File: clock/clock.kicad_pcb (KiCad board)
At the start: 2 copper layers, 176.8 x 81.3 mm, 341 parts, among them P101 CONN_01X03, P102 CONN_FAN_PWM, P103 XG4A-1631, P301 MCRF, P401 CONN_01X10, Q201 MMBT3904, Q301 BSS138, Q302 BSS138, Q401 BSS138, Q402 BSS138, Q501 BSS138, Q502 BSS138, U201 PCA9306, U202 DAC8830, U203 LMV722, U204 LTC2990, U205 LP3853, U207 NC7SZ125, U301 Adafruit746, U302 MIC5225, U303 PA6H, U401 74LVC541, U501 TPS56428, U502 TPS56428, U503 TPS56428, U601 ADT7410, U602 DS3231, U603 ADT7410, Y202 CX210

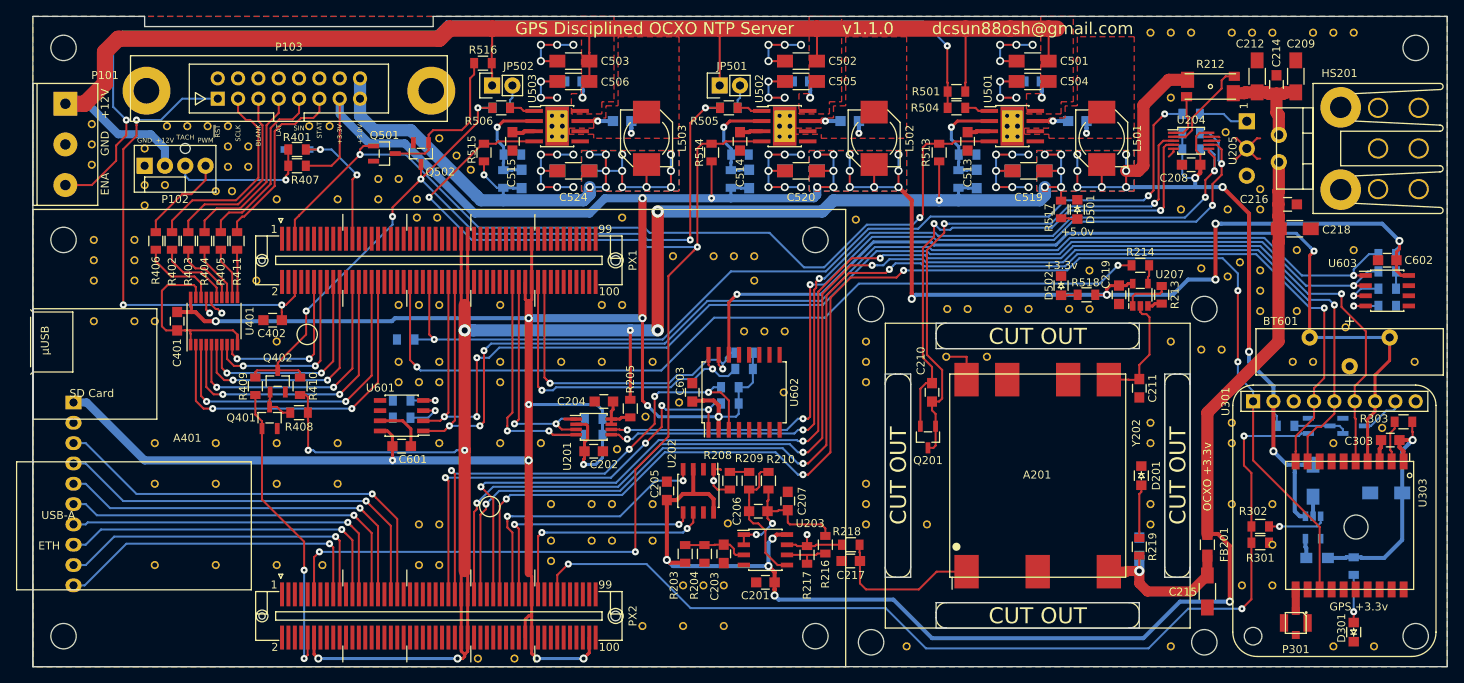
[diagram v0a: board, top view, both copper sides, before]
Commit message: Move power indicator LEDs. Clean up test points and silkscreen. Move the gate of Q302 to the other side of R301.
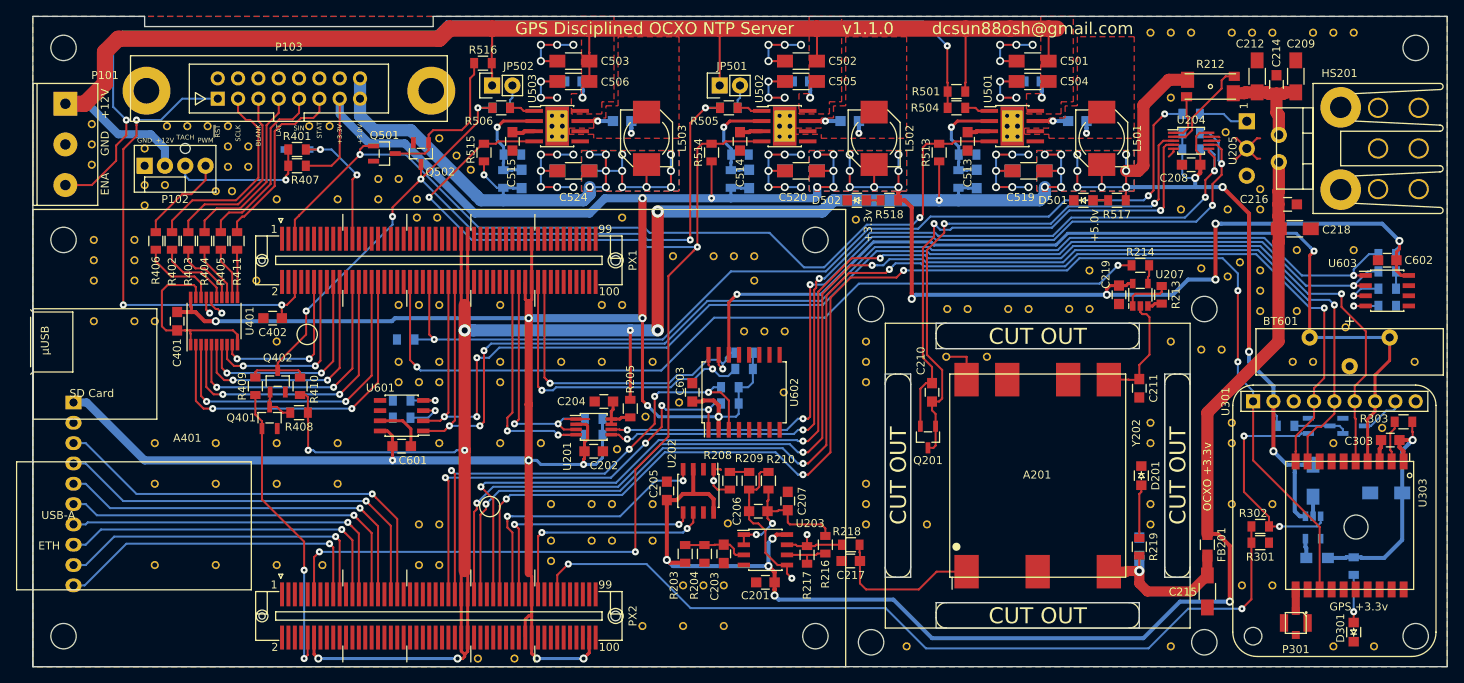
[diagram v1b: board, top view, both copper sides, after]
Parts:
- removed the REF** at (345.4, 231.1)
- moved D502 27.7 mm to (293.5, 188.1), turned to 0 degrees
- moved R518 27.3 mm to (297.6, 188.1)
- moved R517 7.08 mm to (326.0, 188.1), turned to 180 degrees
- moved D501 1.37 mm to (321.8, 188.1), turned to 0 degrees
- moved C402 0.25 mm to (220.5, 202.8)
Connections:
- Q302 pad 1: /gps/ENA -> /gps/ENABLE
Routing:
- net /gps/ENABLE: track 7.47 -> 28.2 mm, vias 1 -> 2
- net /gps/ENA: track 125.6 -> 105.8 mm, vias 3 -> 2
- net VCC: track 490.2 -> 485.8 mm, vias 30 -> 29
- net /ocxo/DAC_OUT_DIV: track 16.8 -> 18.7 mm, vias 0 -> 1
- net GND: track 141.9 -> 143.6 mm
- net /microzed/OCXO_SDA: track 32.4 -> 31.1 mm
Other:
- board text added: "DAC_OUT_DIV"
- board text added: "~RTC_INT~"

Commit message: Connect temperature sensor interrupt to FPGA.
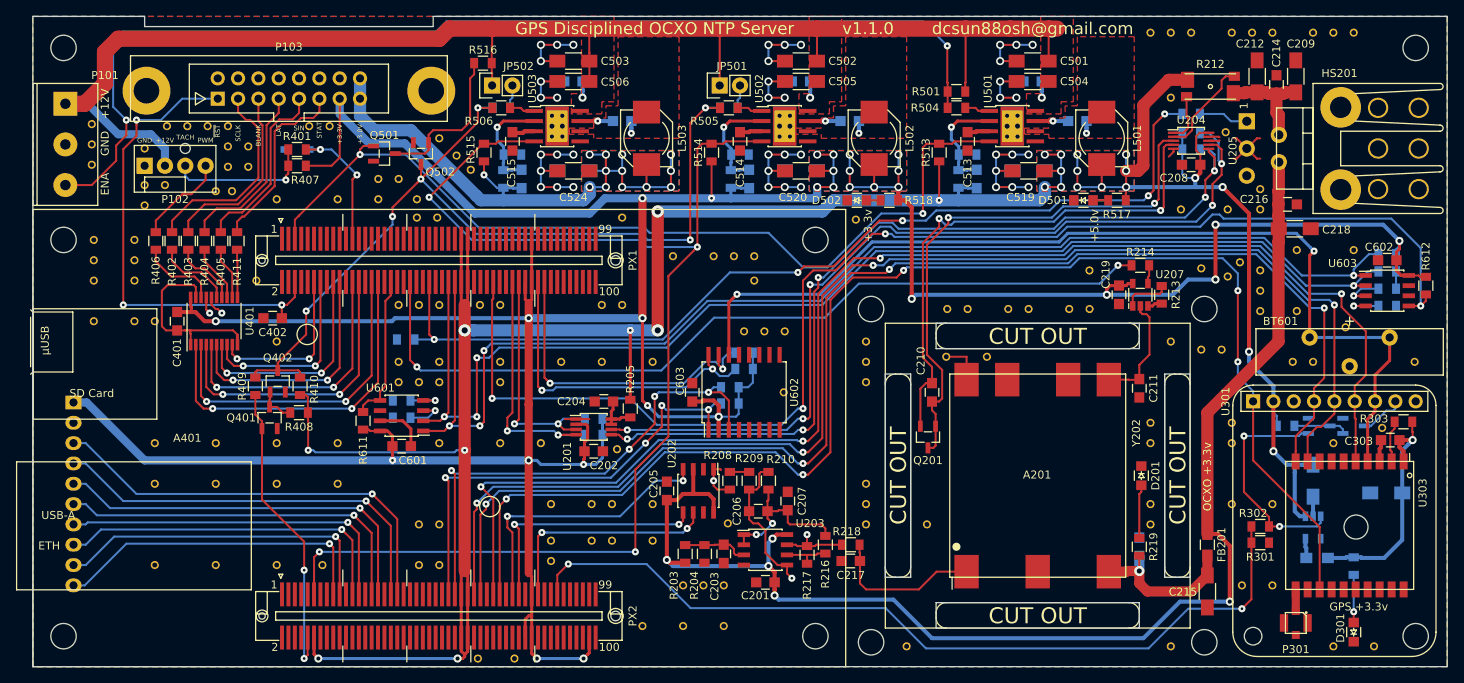
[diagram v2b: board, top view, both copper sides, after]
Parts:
- removed the REF** at (271.3, 213.4)
- removed the REF** at (267.1, 215.1)
- added R611: 1.00K, local:R_0805_HandSoldering, F.Cu at (231.8, 215.6)
- added R612: 1.00K, local:R_0805_HandSoldering, F.Cu at (364.6, 198.8)
- added REF**: Stitching_Via_40x24mil, local:Stitching_Via_40x24mil, F.Cu at (246.4, 201.2)
- R609, R610: value 10.0K -> 1.00K
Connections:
- net /rtctemp/~INT~ renamed /microzed/~INT~0
- PX1 pad 36: /microzed/PX1_LVDS_9_P -> /microzed/~INT~1
- PX1 pad 68: /microzed/PX1_LVDS_19_P -> /microzed/~INT~2
- U601 pad 5: Net-(U601-Pad5) -> /microzed/~INT~1
- U603 pad 5: Net-(U603-Pad5) -> /microzed/~INT~2
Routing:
- net /microzed/~INT~2: track 0.00 -> 164.8 mm, vias 0 -> 4
- net /microzed/~INT~1: track 0.00 -> 18.6 mm
- net VCC: track 485.8 -> 490.0 mm
- net /ocxo/ENA: vias 3 -> 5

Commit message: Clean up some of the trace routing. Update gerber files.
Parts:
- added REF**: Stitching_Via_40x24mil, local:Stitching_Via_40x24mil, F.Cu at (256.5, 201.2)
- added REF**: Stitching_Via_40x24mil, local:Stitching_Via_40x24mil, F.Cu at (229.9, 180.3)
- moved R217 2.41 mm to (289.7, 232.4)
- moved R216 2.29 mm to (287.3, 231.1)
- moved R206 0.25 mm to (237.1, 205.7)
- moved C217 0.13 mm to (292.9, 233.2)
- moved R218 0.13 mm to (292.9, 231.1)
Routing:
- net GND: track 143.6 -> 161.8 mm
- net /ocxo/BUF_VGND_1.65V: track 20.0 -> 17.6 mm
- net VXO: track 165.4 -> 163.2 mm
- net VCC: track 490.0 -> 488.7 mm
- net /ocxo/DAC_OUT: track 5.26 -> 4.29 mm
- net /power/+3.0V: track 76.9 -> 76.1 mm
- net VIN: track 352.4 -> 351.6 mm

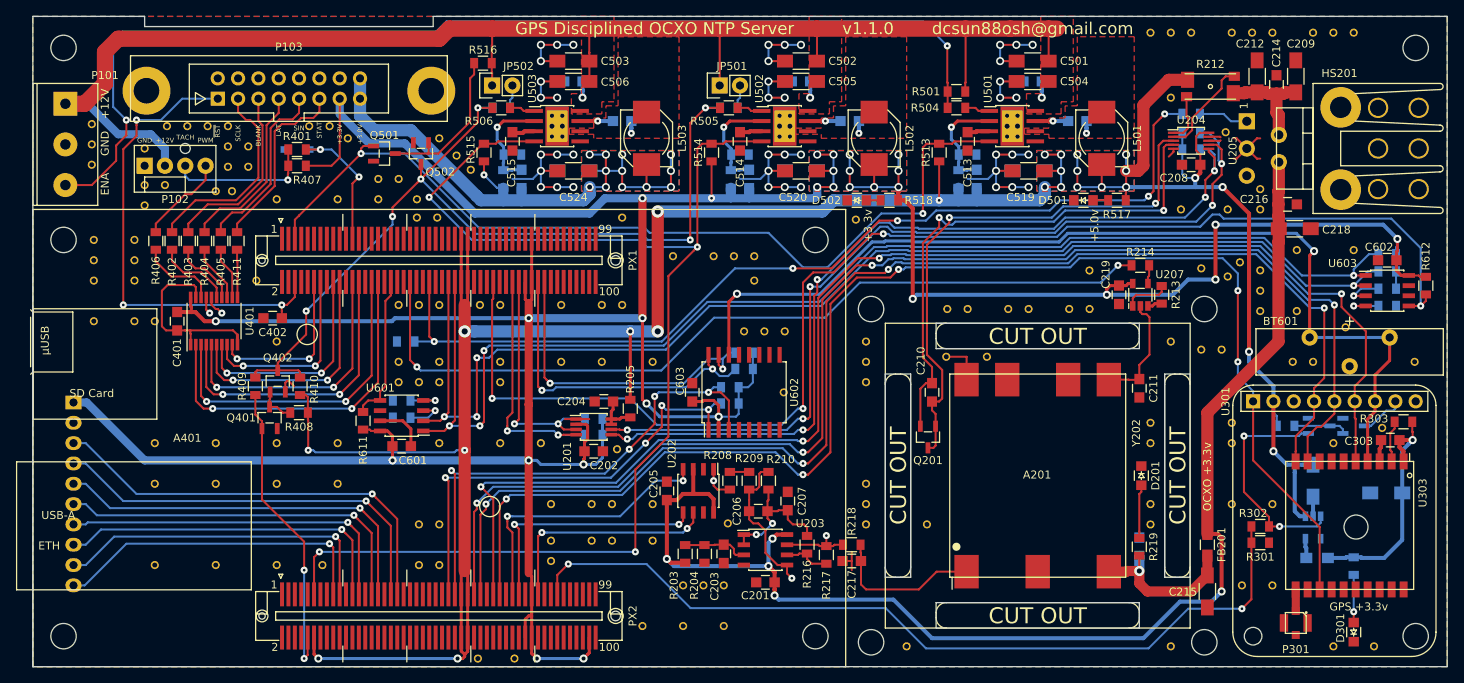
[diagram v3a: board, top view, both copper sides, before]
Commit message: Improve clearance around mounting hole.
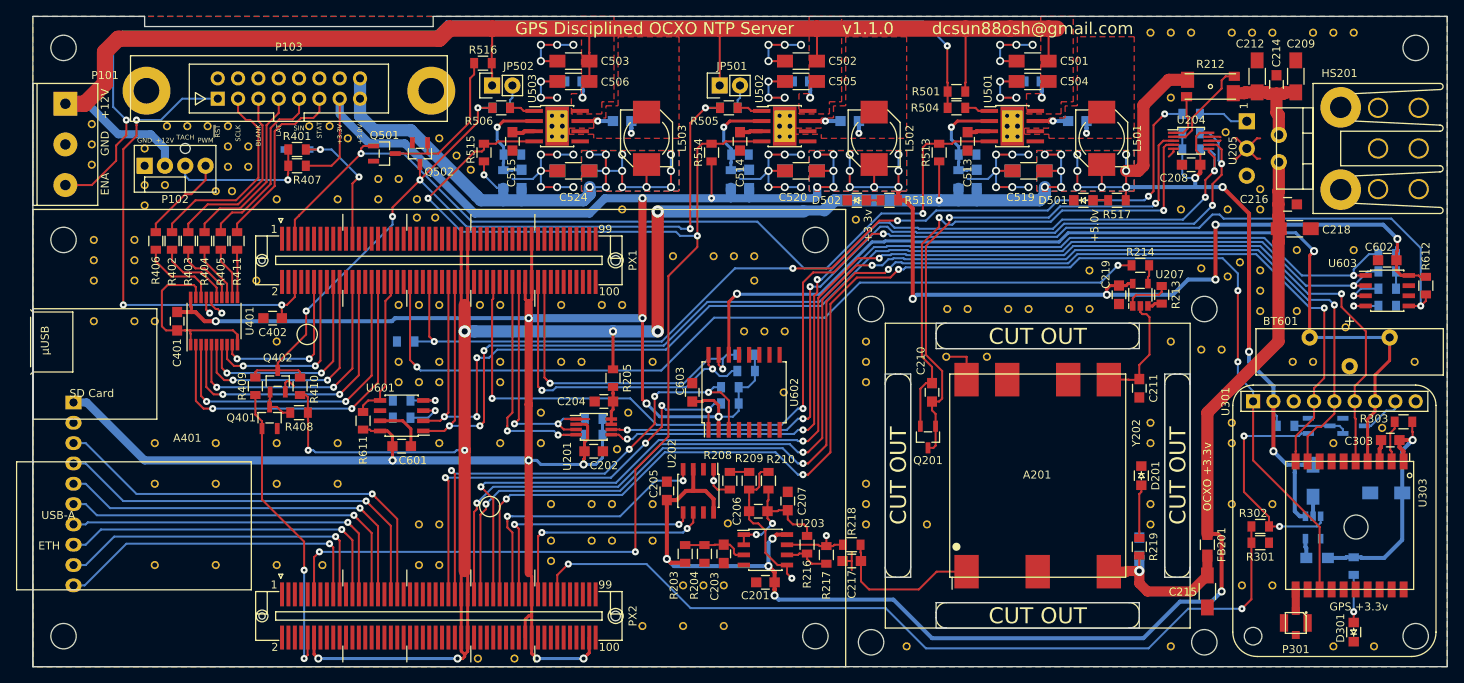
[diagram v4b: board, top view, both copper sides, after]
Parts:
- removed the REF** at (264.2, 190.2)
- added REF**: Stitching_Via_40x24mil, local:Stitching_Via_40x24mil, F.Cu at (264.2, 189.2)
- added REF**: Stitching_Via_40x24mil, local:Stitching_Via_40x24mil, F.Cu at (254.0, 214.6)
- added REF**: Stitching_Via_40x24mil, local:Stitching_Via_40x24mil, F.Cu at (264.9, 214.6)
- moved R205 4.38 mm to (263.0, 210.3)
- moved REF** 2.54 mm to (259.1, 208.3)
- moved R603 0.36 mm to (279.7, 207.4)
- moved R604 0.36 mm to (279.7, 209.4)
- moved REF** 0.25 mm to (240.8, 190.2)
- moved Q502 0.13 mm to (238.9, 182.2)
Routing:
- net VIN: track 351.6 -> 348.1 mm
- net /microzed/+1.8V_PG: track 113.5 -> 111.7 mm
- net /ocxo/LV_ENA: track 5.40 -> 4.77 mm

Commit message: Separate RTC interrupt to allow for different IO register clock domain.
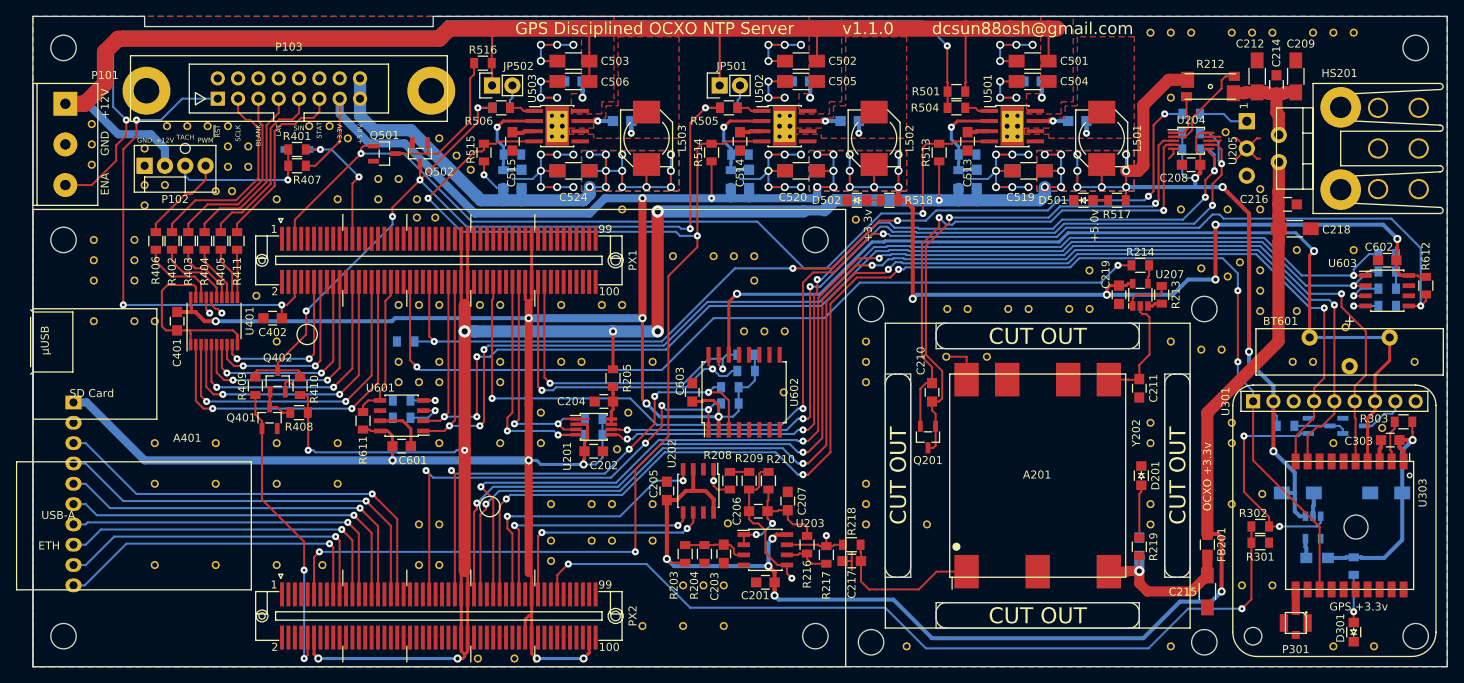
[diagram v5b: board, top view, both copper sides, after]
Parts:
- moved C301 2.44 mm to (348.6, 224.7), turned to 0 degrees
- moved REF** 1.91 mm to (218.4, 200.0)
- moved REF** 1.80 mm to (344.2, 224.8)
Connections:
- PX2 pad 47: /microzed/PX2_LVDS_10_P -> /rtctemp/32KHZ
- PX2 pad 53: /rtctemp/32KHZ -> /microzed/PX2_LVDS_12_P
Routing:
- net /rtctemp/32KHZ: track 57.6 -> 61.2 mm
- net VIN: track 348.1 -> 346.8 mm
- net VCC: track 488.4 -> 487.2 mm
- net GND: track 161.8 -> 162.6 mm
